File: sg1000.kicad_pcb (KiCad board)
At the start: 2 copper layers, 52 parts, among them CN1 Conn_01x07_Female, J1 USB-B1HSB6, Q1c1 2n3906, SW1 Pause Key, SW2 Power Toggle, U1 SG-1000-Cart, U10 PLCCZ80, U100 74HCT574, U101 74HCT574, U102 74HCT574, U103 AS6C62256-DIP, U11 AS6C62256-DIP, U12 TMS9918A, U13 74LS139, U16 74LS32, U18 74LS257, U21 74LS257, U3 SN76489AN, U99 74HCT04, X2 10.73863MHz

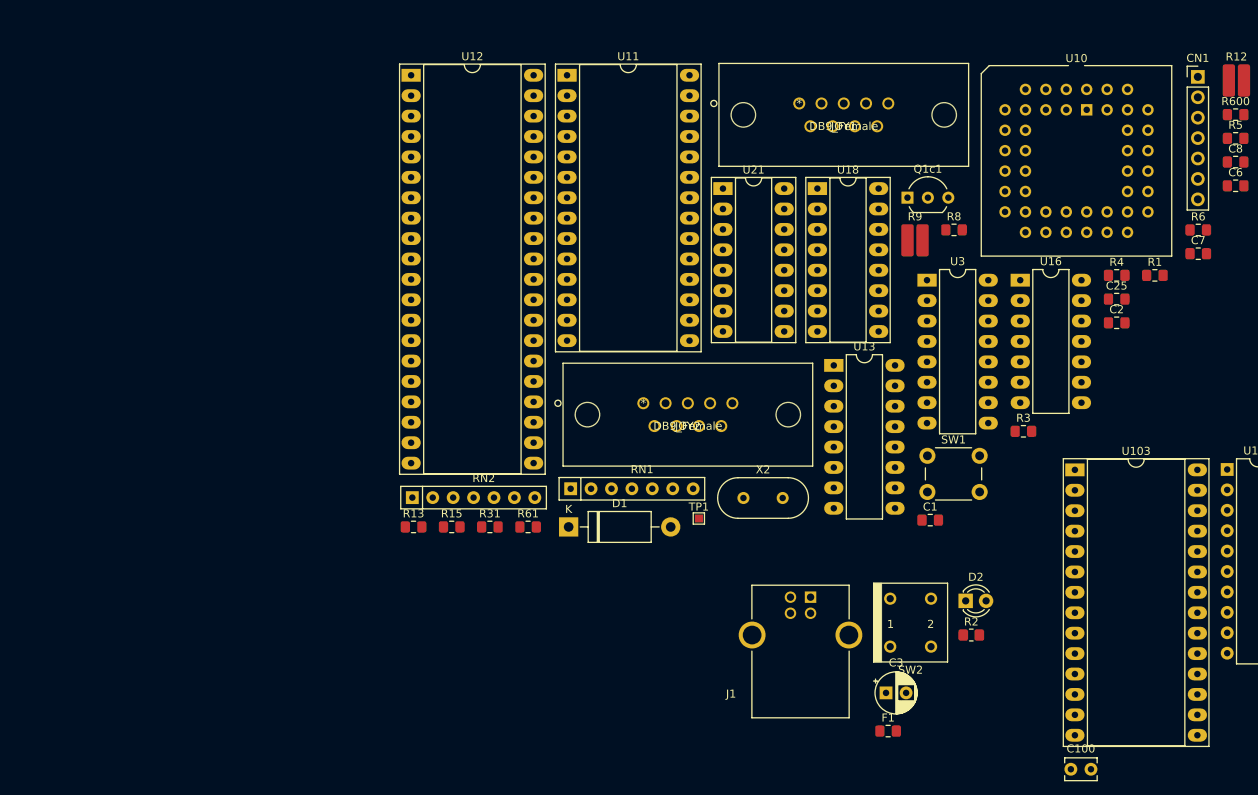
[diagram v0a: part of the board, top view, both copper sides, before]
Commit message: Layout started, and abandoned for now
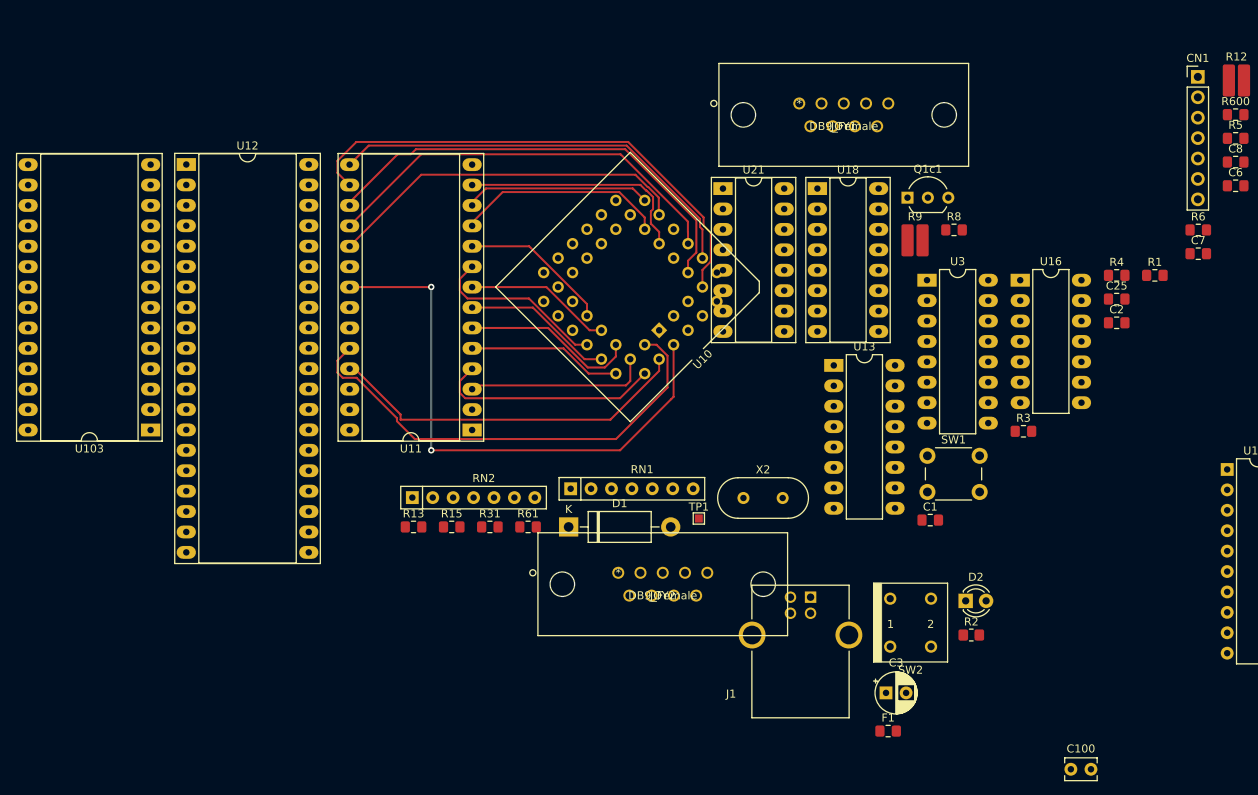
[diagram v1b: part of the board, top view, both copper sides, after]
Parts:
- moved U103 115.1 mm to (47.0, 104.8), turned to 180 degrees
- moved U10 59.9 mm to (110.3, 92.4), turned to -135 degrees
- moved U11 45.7 mm to (87.0, 104.8), turned to 180 degrees
- moved U12 30.1 mm to (51.4, 71.8)
- moved JOY2 21.3 mm to (105.2, 122.6)
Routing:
- net /A10: track 0.00 -> 69.9 mm, vias 0 -> 2
- net /D4: track 0.00 -> 63.5 mm
- net /A9: track 0.00 -> 58.4 mm
- net /D5: track 0.00 -> 56.9 mm
- net /D3: track 0.00 -> 53.4 mm
- net /D6: track 0.00 -> 52.0 mm
- net /D7: track 0.00 -> 45.5 mm
- net /A8: track 0.00 -> 45.5 mm
- net /D2: track 0.00 -> 29.5 mm
- net /A6: track 0.00 -> 28.2 mm
- net /D0: track 0.00 -> 26.2 mm
- net /D1: track 0.00 -> 23.2 mm
- net /A7: track 0.00 -> 22.8 mm
- net /A1: track 0.00 -> 22.2 mm
- net /A4: track 0.00 -> 22.0 mm
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
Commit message: I'm gonna need an outline before we continue
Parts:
- R12, R9: footprint Resistor_SMD:R_0815_2038Metric_Pad1.53x4.00mm_HandSolder -> Resistor_SMD:R_0805_2012Metric_Pad1.20x1.40mm_HandSolder
- moved U99 190.8 mm to (22.9, 116.8)
- moved C100 161.9 mm to (21.0, 66.7)
- moved U101 161.2 mm to (44.5, 140.7), turned to 180 degrees
- moved U100 156.3 mm to (36.8, 89.2)
- moved C8 140.8 mm to (51.9, 125.2), turned to 90 degrees
- moved U102 138.8 mm to (44.5, 84.3), turned to 180 degrees
- moved CN1 133.1 mm to (83.8, 155.6), turned to 90 degrees
- moved C7 126.2 mm to (58.5, 125.2), turned to 90 degrees
- moved JOY1 106.8 mm to (97.2, 166.5), turned to 180 degrees
- moved R8 102.0 mm to (55.1, 124.2)
- moved J1 87.7 mm to (118.7, 43.1)
- moved R2 87.4 mm to (63.5, 148.0), turned to 90 degrees
- moved D2 81.9 mm to (69.8, 149.2), turned to 90 degrees
- moved U3 80.0 mm to (68.8, 57.6), turned to -90 degrees
- moved SW2 79.9 mm to (67.3, 158.5)
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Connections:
- net Net-(C3-Pad1) renamed /Fused_Power
- net Net-(F1-Pad1) renamed /USB_Power
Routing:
- net GND: track 0.00 -> 86.9 mm
- net /JOY2_DOWN: track 0.00 -> 64.2 mm, vias 0 -> 2
- net /JOY2_UP: track 0.00 -> 63.5 mm, vias 0 -> 1
- net /A0: track 18.7 -> 77.7 mm, vias 0 -> 1
- net /JOY1_LEFT: track 0.00 -> 57.0 mm, vias 0 -> 1
- net /JOY1_RIGHT: track 0.00 -> 51.8 mm
- net /JOY1_DOWN: track 0.00 -> 48.9 mm, vias 0 -> 2
- net /~{WR}: track 0.00 -> 43.3 mm, vias 0 -> 2
- net /~{INT}: track 0.00 -> 41.9 mm
- net /JOY1_UP: track 0.00 -> 37.2 mm
- net /~{RD}: track 0.00 -> 36.3 mm, vias 0 -> 1
- net /JOY2_BUTTON1: track 0.00 -> 36.0 mm, vias 0 -> 1
- net /~{RESET}: track 0.00 -> 34.0 mm
- net /~{JOY_SEL}: track 0.00 -> 33.0 mm
- net +5V: track 0.00 -> 30.9 mm
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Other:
- board text added: "BS-1000"
- board text added: "by leadedsolder.com 2022"
- board text added: "v0.1"

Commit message: Output ports
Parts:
- added C4: 0.1µF, Capacitor_SMD:C_0805_2012Metric_Pad1.18x1.45mm_HandSolder, F.Cu at (71.8, 49.5)
- added C5: 220µF, Capacitor_THT:CP_Radial_D6.3mm_P2.50mm, F.Cu at (74.9, 44.1)
- added C9: 0.1µF, Capacitor_SMD:C_0805_2012Metric_Pad1.18x1.45mm_HandSolder, F.Cu at (82.4, 41.7)
- added J2: RCJ-014, Jacks:CUI_RCJ-017, F.Cu at (57.1, 47.0)
- added J3: RCJ-013, Jacks:CUI_RCJ-017, F.Cu at (41.9, 47.0)
- added Q1: 2n4401, Package_TO_SOT_THT:TO-92_Inline_Wide, F.Cu at (62.7, 47.6)
- added R10: 1kΩ, Resistor_SMD:R_0805_2012Metric_Pad1.20x1.40mm_HandSolder, F.Cu at (81.3, 49.5)
- added R11: 470Ω, Resistor_SMD:R_0805_2012Metric_Pad1.20x1.40mm_HandSolder, F.Cu at (76.5, 49.5)
- added R14: 75Ω, Resistor_SMD:R_0805_2012Metric_Pad1.20x1.40mm_HandSolder, F.Cu at (86.0, 44.7)
- added R7: 0Ω, Resistor_SMD:R_0805_2012Metric_Pad1.20x1.40mm_HandSolder, F.Cu at (90.8, 41.6)
- added SP1: 74LS00, Package_DIP:DIP-14_W7.62mm, F.Cu at (62.8, 27.0)
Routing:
- net /~{VDP_WR}: track 0.00 -> 34.0 mm
- net /~{RESET}: track 34.0 -> 0.00 mm

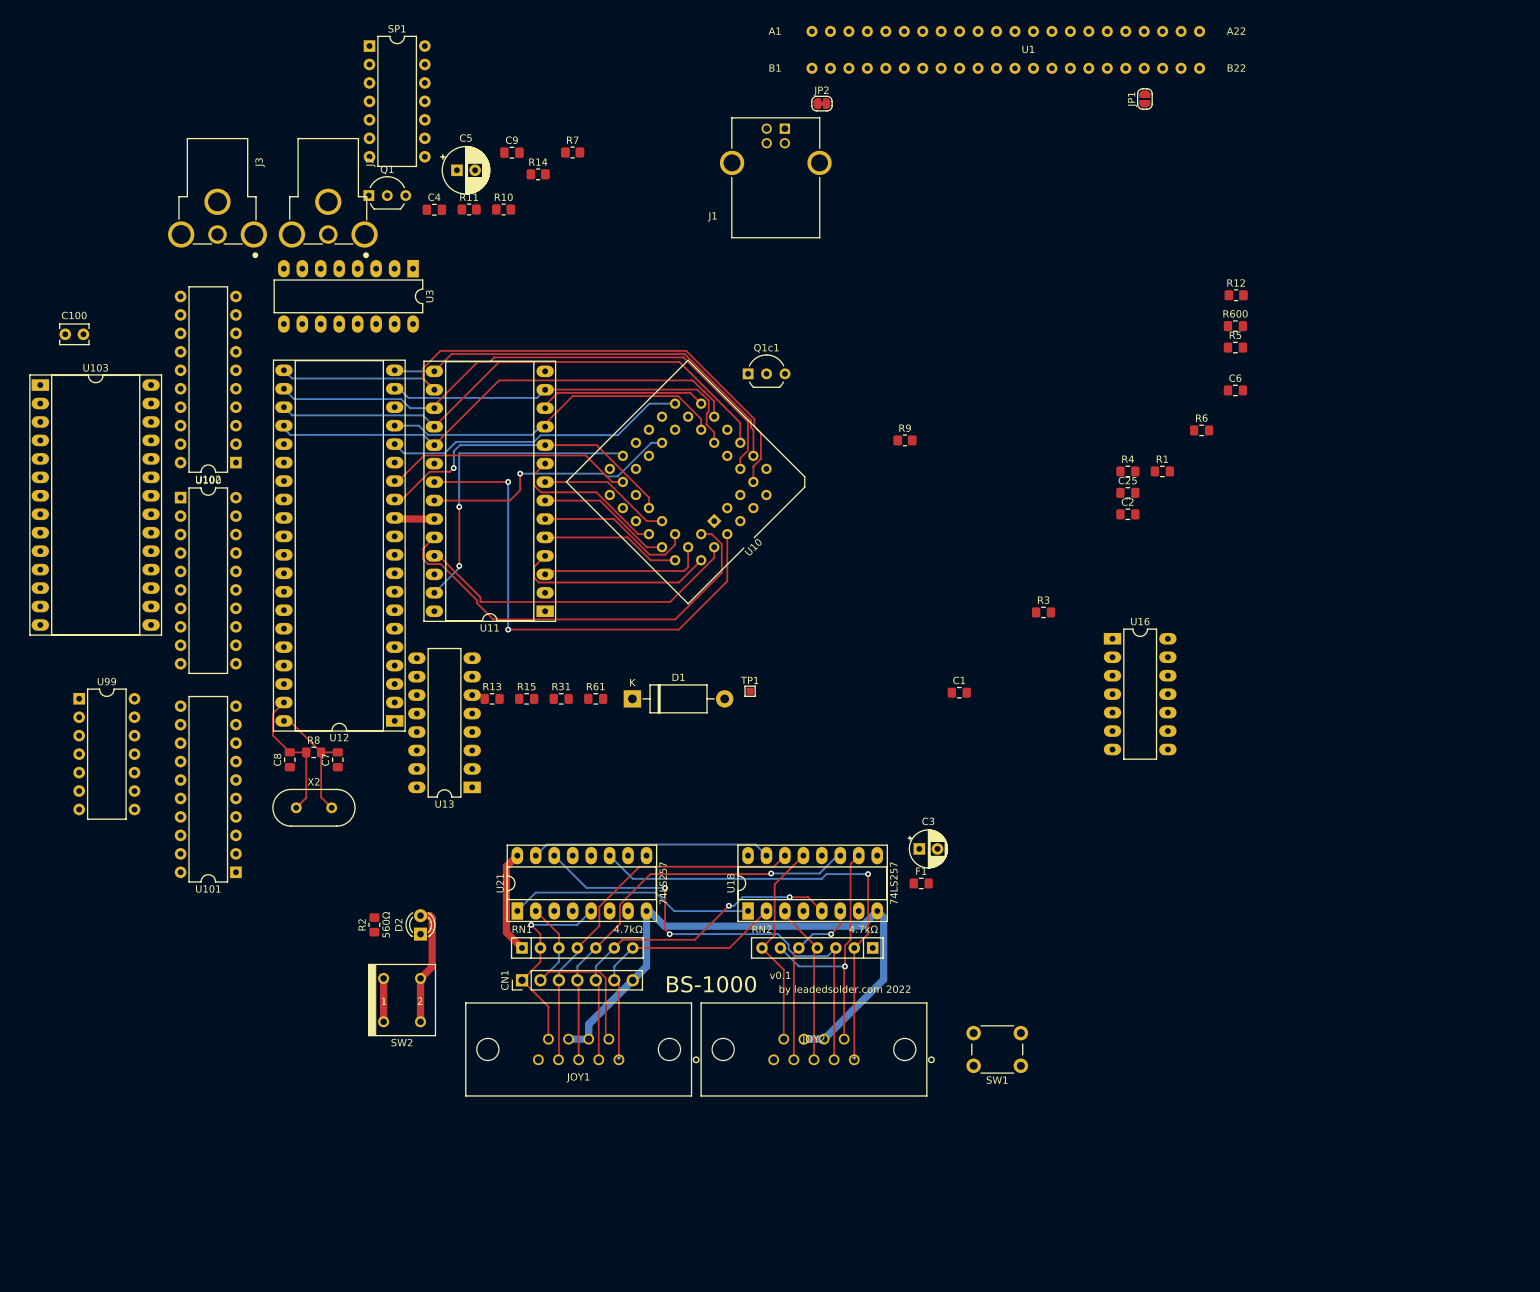
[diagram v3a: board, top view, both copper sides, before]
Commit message: Cart slot revision
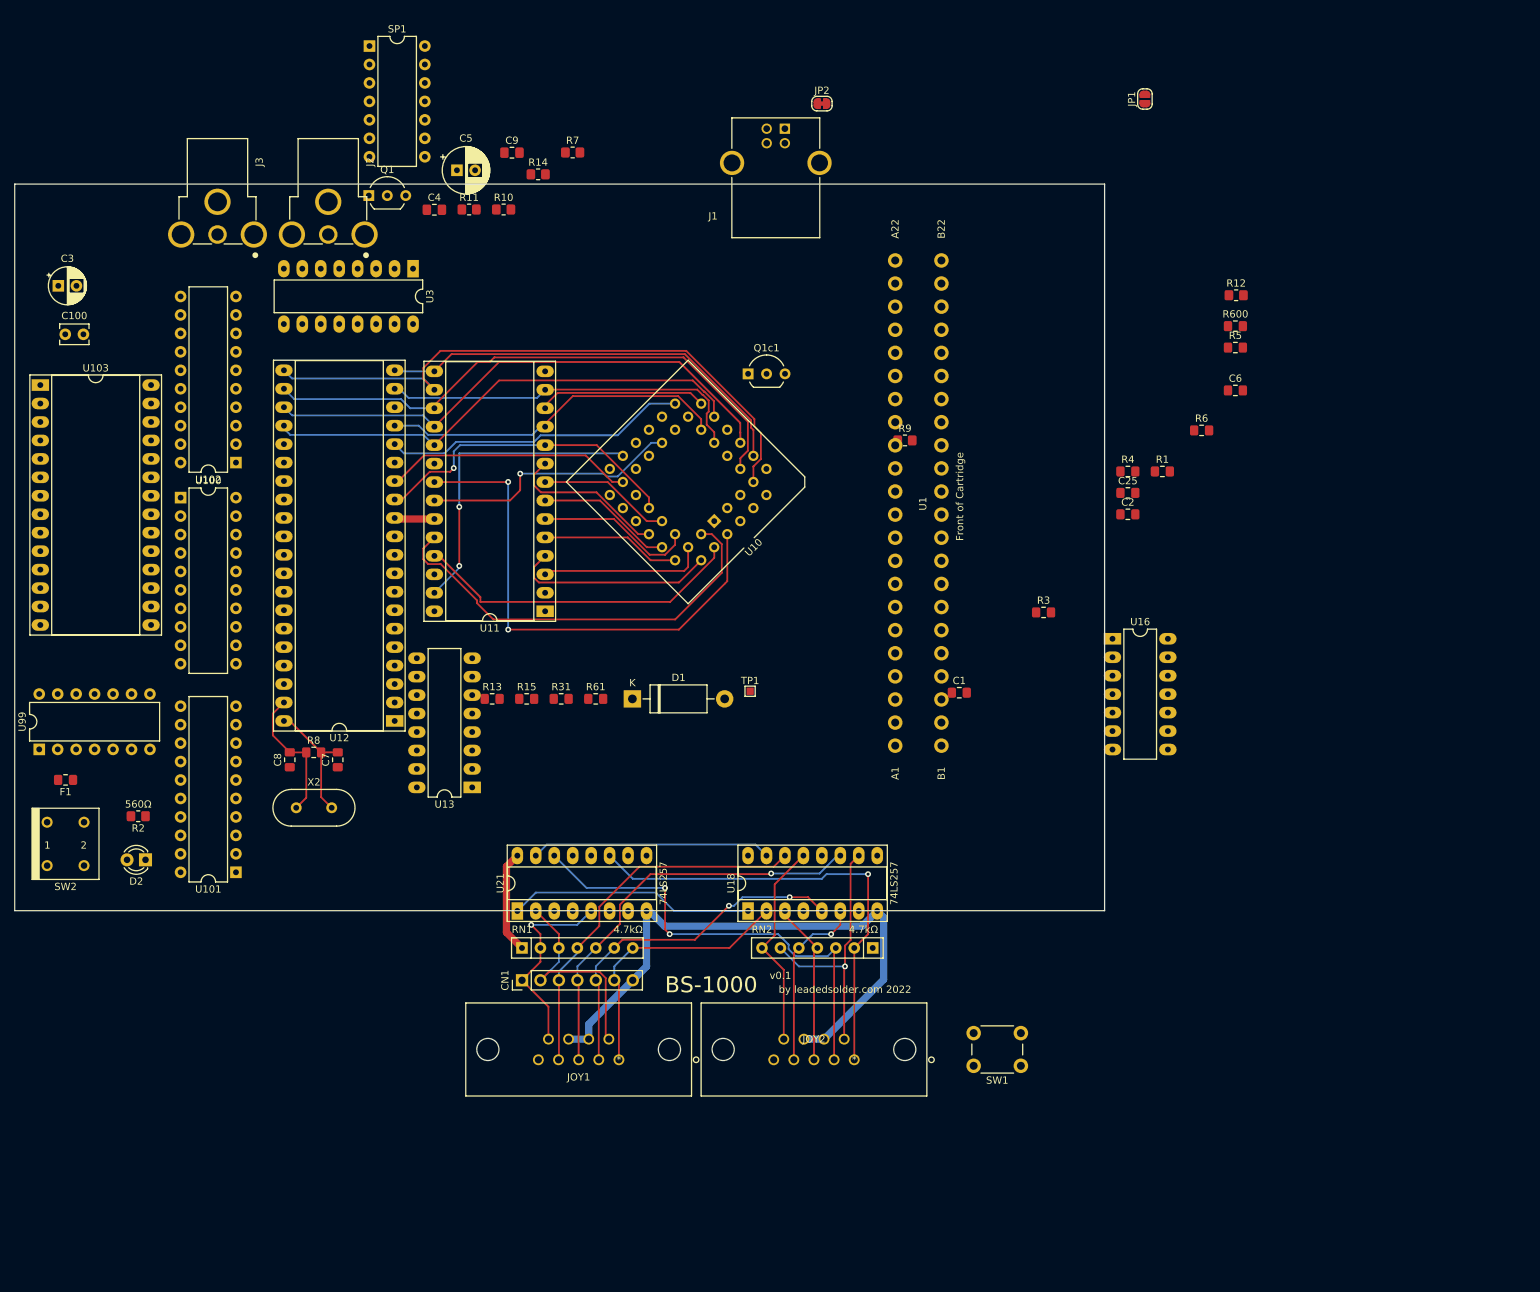
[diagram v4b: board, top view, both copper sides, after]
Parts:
- moved C3 141.6 mm to (20.0, 60.0)
- moved F1 118.6 mm to (21.0, 128.0), turned to 180 degrees
- moved U1 62.5 mm to (139.0, 89.0), turned to 90 degrees
- moved SW2 51.1 mm to (21.0, 137.0)
- moved D2 39.2 mm to (32.0, 139.0), turned to 180 degrees
- moved R2 35.8 mm to (31.0, 133.0), turned to 180 degrees
- moved U99 8.87 mm to (17.4, 123.8), turned to 90 degrees
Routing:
- net +5V: track 30.9 -> 14.2 mm
- net /Fused_Power: track 5.97 -> 0.00 mm
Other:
- board outline added: 150 x 100 mm

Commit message: Add A11 jumper so we can maybe get 2k
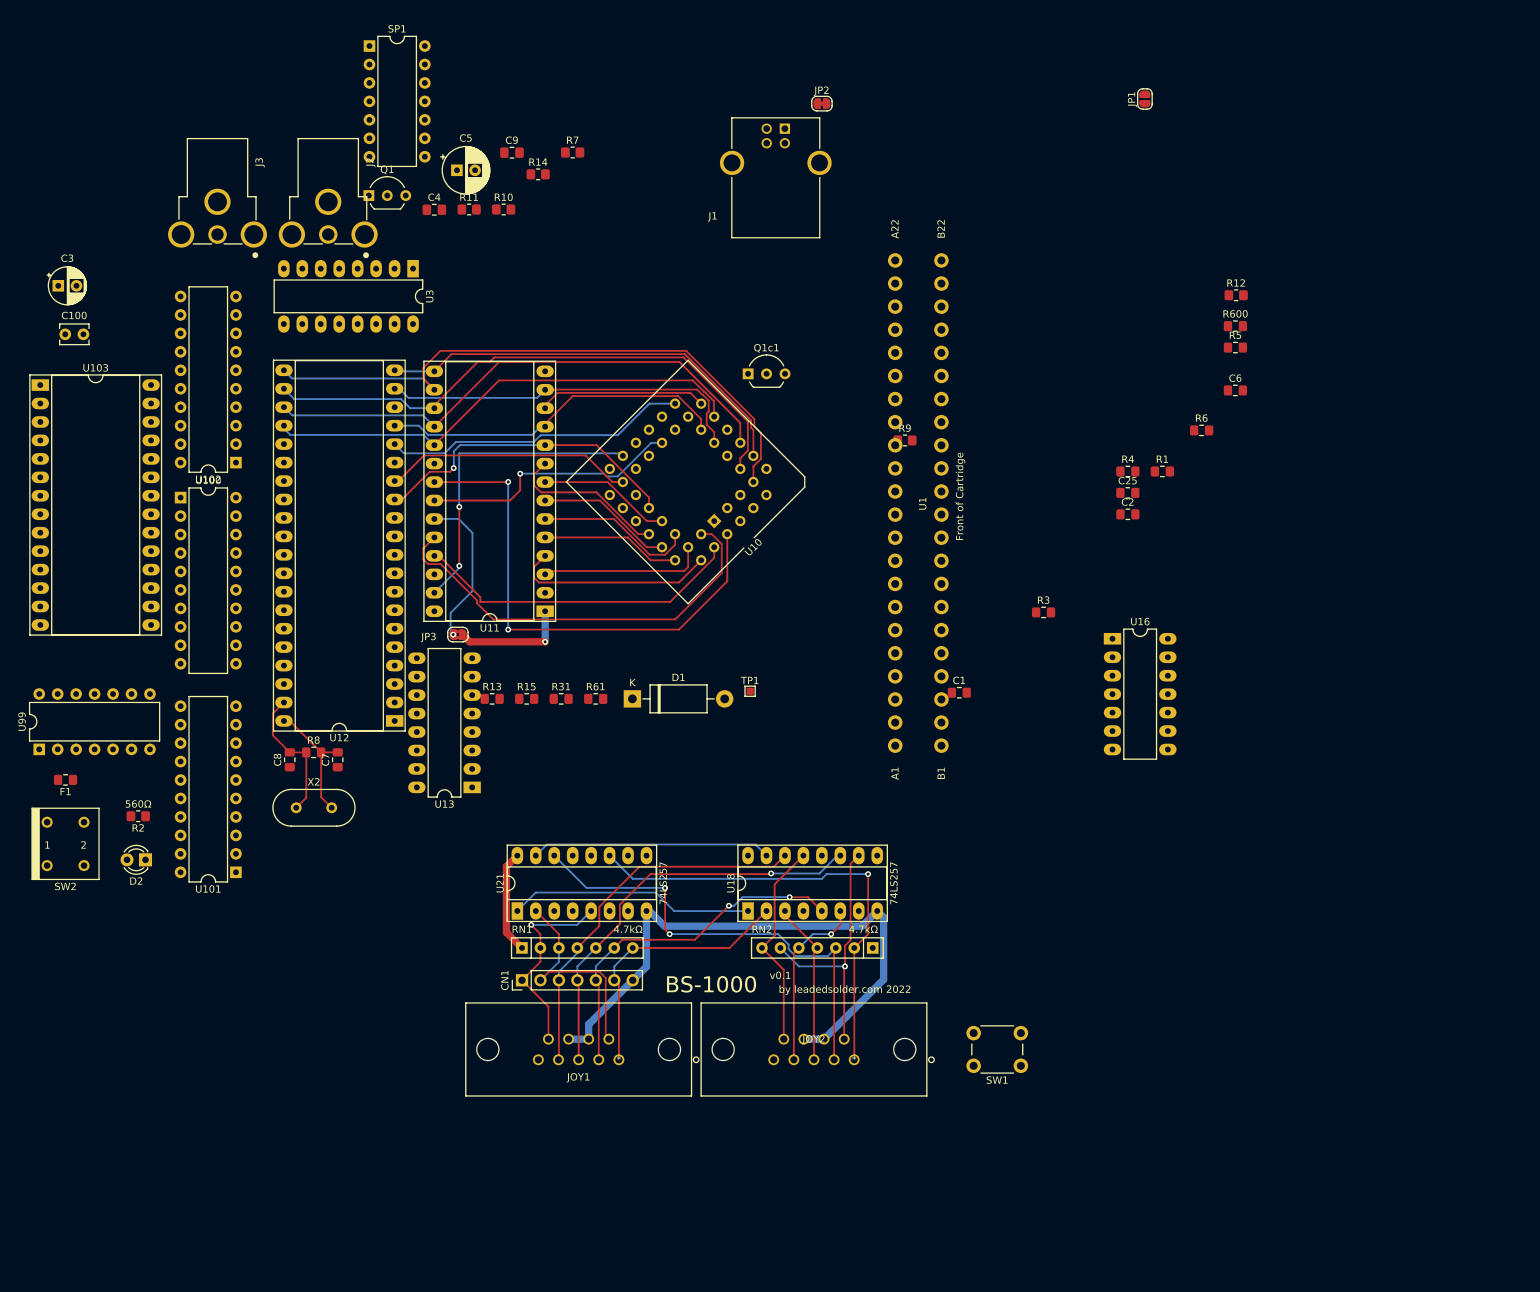
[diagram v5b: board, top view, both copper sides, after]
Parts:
- added JP3: Jumper_2_Bridged, Jumper:SolderJumper-2_P1.3mm_Bridged2Bar_RoundedPad1.0x1.5mm, F.Cu at (75.0, 108.0)
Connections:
- U11 pad 23: GND -> Net-(U11-Pad23)
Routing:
- net /~{VDP_WR}: track 34.0 -> 0.00 mm
- net /~{RESET}: track 0.00 -> 34.0 mm
- net Net-(U11-Pad23): track 0.00 -> 21.4 mm, vias 0 -> 1
- net GND: track 86.9 -> 97.5 mm, vias 0 -> 1
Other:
- board outline removed
- board text added: "a11"
